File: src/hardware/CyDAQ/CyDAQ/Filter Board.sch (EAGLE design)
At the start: 215 parts, among them J1 DCJ0202, J10 Vout_HEADER, J11 5V0_SENSOR, J12 3V3_SENSOR, J13 1V8_SENSOR, J14 BRKOUT_JD, J15 BRKOUT_JC, J16 BRKOUT_JB, J17 BRKOUT_JF, J18 5V0_CONN, J19 3V3_CONN, J2 ZYBO_JF, J20 1V8_CONN, J21 BRKOUT_JD, J22 ZYBO_Power, J23 ZYBO_Power, J3 ZYBO_JE, J4 ZYBO_JD, J5 ZYBO_JC, J6 ZYBO_JB, J7 A_XADC, J8 SJ1-3523N, J9 Vin_HEADER, U1 TPS54531DDARDDA8_3P1X2P4-L, U10 CD74HCT4051, U11 CD74HCT4051, U12 OPA4197, U13 OPA4197, U14 OPA4197, U15 OPA4197, U16 OPA4197, U17 CD74HCT4053, U18 CD74HCT4051, U19 OPA2197, U3 TPS56339, U4 TPS56339, U5 LM43601PWPR, U6 X9258, U7 X9258, U8 X9258, U9 X9258

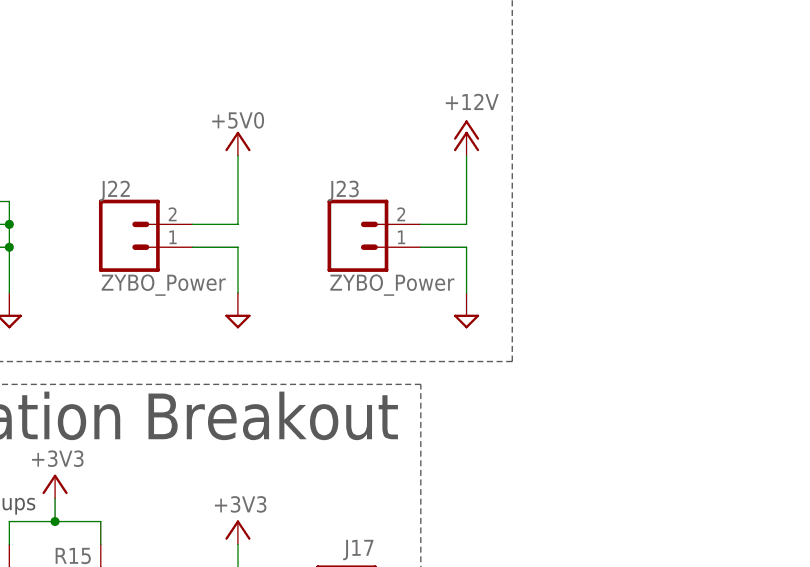
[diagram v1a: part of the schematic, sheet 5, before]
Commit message: Adjusted C3 Silkscreen and added 3D renders
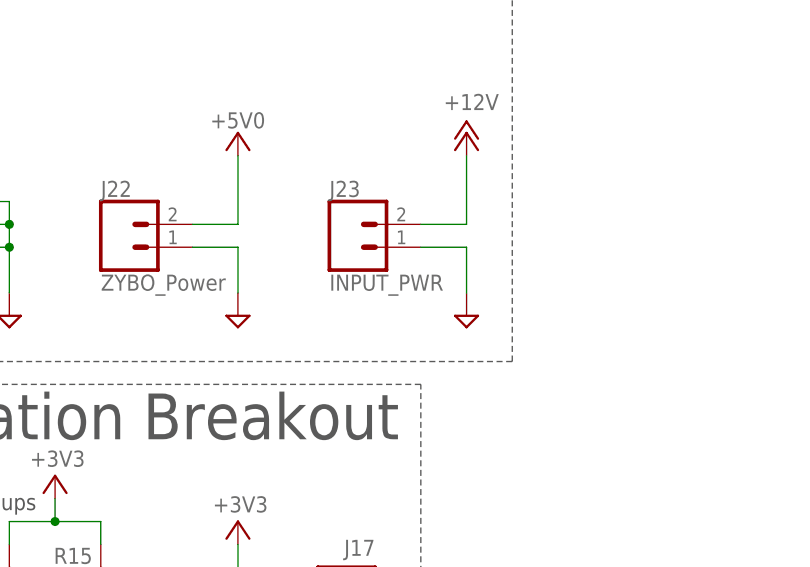
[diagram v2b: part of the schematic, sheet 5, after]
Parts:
- J23: value ZYBO_Power -> INPUT_PWR
- L3: MANUFACTURER_PART_NUMBER (none) -> NLCV32T-2R2M-PFR
